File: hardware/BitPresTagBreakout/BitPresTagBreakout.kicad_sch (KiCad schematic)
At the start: 10 parts, among them J3 Conn_01x17, J4 Conn_01x17, U2 AT25XE321, U3 LPS27HHWTR, U4 adxl362

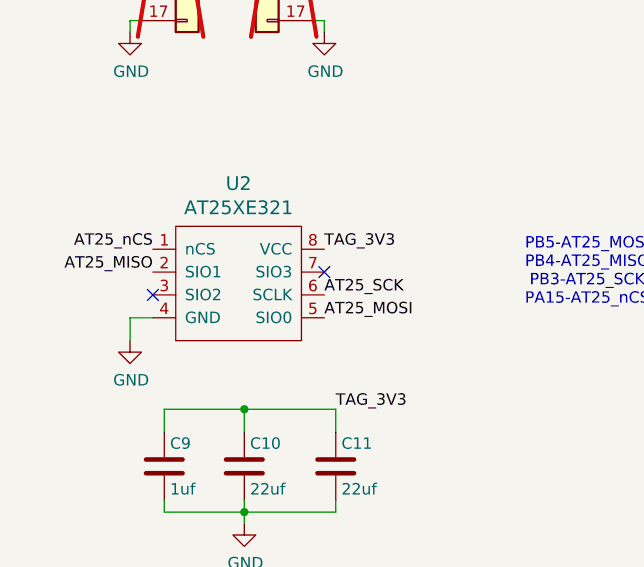
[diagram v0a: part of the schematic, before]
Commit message: checkpoint -- order compass proto board
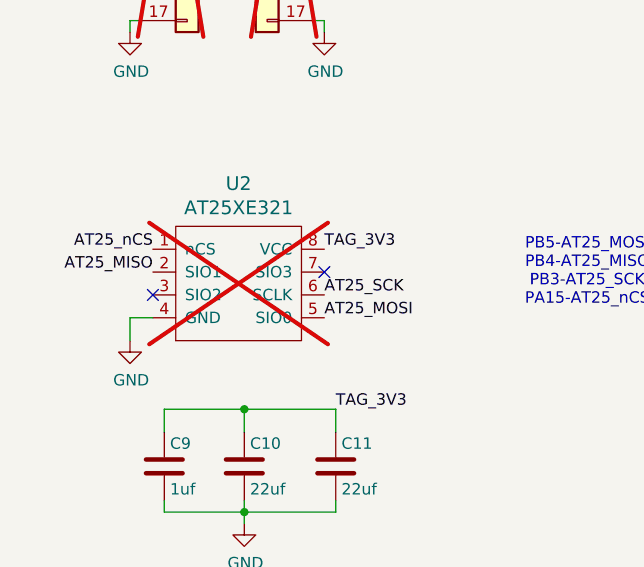
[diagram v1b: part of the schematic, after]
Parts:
- U2: now not fitted
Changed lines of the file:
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@@
 		(in_bom yes)
 		(on_board yes)
-		(dnp no)
+		(dnp yes)
 		(property "Reference" "U2"
 			(at 48.895 115.9002 0)

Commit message: update proto boards
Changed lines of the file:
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@@
 	)
 	(label "rtc_sda"
-		(at 37.465 64.77 180)
+		(at 38.1 64.77 180)
 		(effects
 			(font
@@
 	)
 	(label "rtc_scl"
-		(at 37.465 62.23 180)
+		(at 38.1 62.23 180)
 		(effects
 			(font
@@
 	)
 	(label "PB8"
-		(at 37.465 67.31 180)
+		(at 38.1 67.31 180)
 		(effects
 			(font
@@
 	)
 	(label "PB9"
-		(at 37.465 69.85 180)
-		(effects
-			(font
+		(at 38.1 69.85 180)
+		(effects
+			(font

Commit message: update prototype boards
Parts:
- U3: LCSC C3253631 -> C3010792; MPN LPS27HHTWTR -> LPS27HHWTR
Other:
- note added: "Note: using lower cost lps27 with less accurate temperature sensor for this board."
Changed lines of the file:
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@@
+	)
+	(junction
+		(at 195.58 36.83)
+		(diameter 0)
+		(color 0 0 0 0)
 	)
 	(junction
@@
 	(wire
 		(pts
+			(xy 160.02 68.58) (xy 144.78 68.58)
+		)
+		(stroke
+			(width 0)
+			(type default)
+		)
+	)
+	(wire
+		(pts
 			(xy 57.15 92.71) (xy 64.77 92.71)
 		)
@@
 	(wire
 		(pts
-			(xy 144.78 68.58) (xy 144.78 74.93)
-		)
-		(stroke
-			(width 0)
-			(type default)
-		)
-	)
-	(wire
-		(pts
 			(xy 180.34 97.79) (xy 177.8 97.79)
 		)
@@
 	(wire
 		(pts
+			(xy 144.78 68.58) (xy 144.78 77.47)
+		)
+		(stroke
+			(width 0)
+			(type default)
+		)
+	)
+	(wire
+		(pts
 			(xy 207.01 118.11) (xy 207.01 120.65)
 		)
@@
 	(wire
 		(pts
-			(xy 160.02 68.58) (xy 144.78 68.58)
-		)
-		(stroke
-			(width 0)
-			(type default)
-		)
-	)
-	(wire
-		(pts
 			(xy 135.89 118.11) (xy 135.89 120.65)
 		)
@@
 			(width 0)
 			(type default)
+		)
+	)
+	(text "Note: using lower cost lps27 with less accurate\ntemperature sensor for this board."
+		(exclude_from_sim no)
+		(at 179.07 81.28 0)
+		(effects
+			(font
+				(size 1.27 1.27)
+			)
 		)
 	)
@@
 			)
 		)
-		(property "MPN" "LPS27HHTWTR"
+		(property "MPN" "LPS27HHWTR"
 			(at 158.75 60.96 0)
 			(effects
@@
 			)
 		)
-		(property "LCSC" "C3253631"
+		(property "LCSC" "C3010792"
 			(at 160.02 63.5 0)
 			(effects
@@
 				(path "/dc006d87-46a7-47a2-9c65-845f7016dec0"
 					(reference "U4")
+					(unit 1)
+				)
+			)
+		)
+	)
+	(symbol
+		(lib_id "power:PWR_FLAG")
+		(at 195.58 36.83 0)
+		(unit 1)
+		(exclude_from_sim no)
+		(in_bom yes)
+		(on_board yes)
+		(dnp no)
+		(fields_autoplaced yes)
+		(property "Reference" "#FLG2"
+			(at 195.58 34.925 0)
+			(effects
+				(font
+					(size 1.27 1.27)
+				)
+				(hide yes)
+			)
+		)
+		(property "Value" "PWR_FLAG"
+			(at 195.58 31.75 0)
+			(effects
+				(font
+					(size 1.27 1.27)
+				)
+			)
+		)
+		(property "Footprint" ""
+			(at 195.58 36.83 0)
+			(effects
+				(font
+					(size 1.27 1.27)
+				)
+				(hide yes)
+			)
+		)
+		(property "Datasheet" "~"
+			(at 195.58 36.83 0)
+			(effects
+				(font
+					(size 1.27 1.27)
+				)
+				(hide yes)
+			)
+		)
+		(property "Description" "Special symbol for telling ERC where power comes from"
+			(at 195.58 36.83 0)
+			(effects
+				(font
+					(size 1.27 1.27)
+				)
+				(hide yes)
+			)
+		)
+		(pin "1"
+		)
+		(instances
+			(project ""
+				(path "/dc006d87-46a7-47a2-9c65-845f7016dec0"
+					(reference "#FLG2")
 					(unit 1)
 				)
@@
 		(lib_name "GND_10")
 		(lib_id "power:GND")
-		(at 144.78 74.93 0)
+		(at 144.78 77.47 0)
 		(unit 1)
 		(exclude_from_sim no)
@@
 		(dnp no)
 		(property "Reference" "#PWR1"
+			(at 144.78 83.82 0)
+			(effects
+				(font
+					(size 1.27 1.27)
+				)
+				(hide yes)
+			)
+		)
+		(property "Value" "GND"
 			(at 144.78 81.28 0)
 			(effects
@@
 					(size 1.27 1.27)
 				)
-				(hide yes)
-			)
-		)
-		(property "Value" "GND"
-			(at 144.78 78.74 0)
-			(effects
-				(font
-					(size 1.27 1.27)
-				)
 			)
 		)
 		(property "Footprint" ""
-			(at 144.78 74.93 0)
+			(at 144.78 77.47 0)
 			(effects
 				(font
@@
 		)
 		(property "Datasheet" ""
-			(at 144.78 74.93 0)
+			(at 144.78 77.47 0)
 			(effects
 				(font
@@
 		)
 		(property "Description" "Power symbol creates a global label with name \"GND\" , ground"
-			(at 144.78 74.93 0)
-			(effects
-				(font
+			(at 144.78 77.47 0)
+			(effects
+				(font
